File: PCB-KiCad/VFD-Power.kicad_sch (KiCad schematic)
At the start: 15 parts, among them IC1 74132D, IC3 ZXBM5210, U3 R-78B5.0-2.0

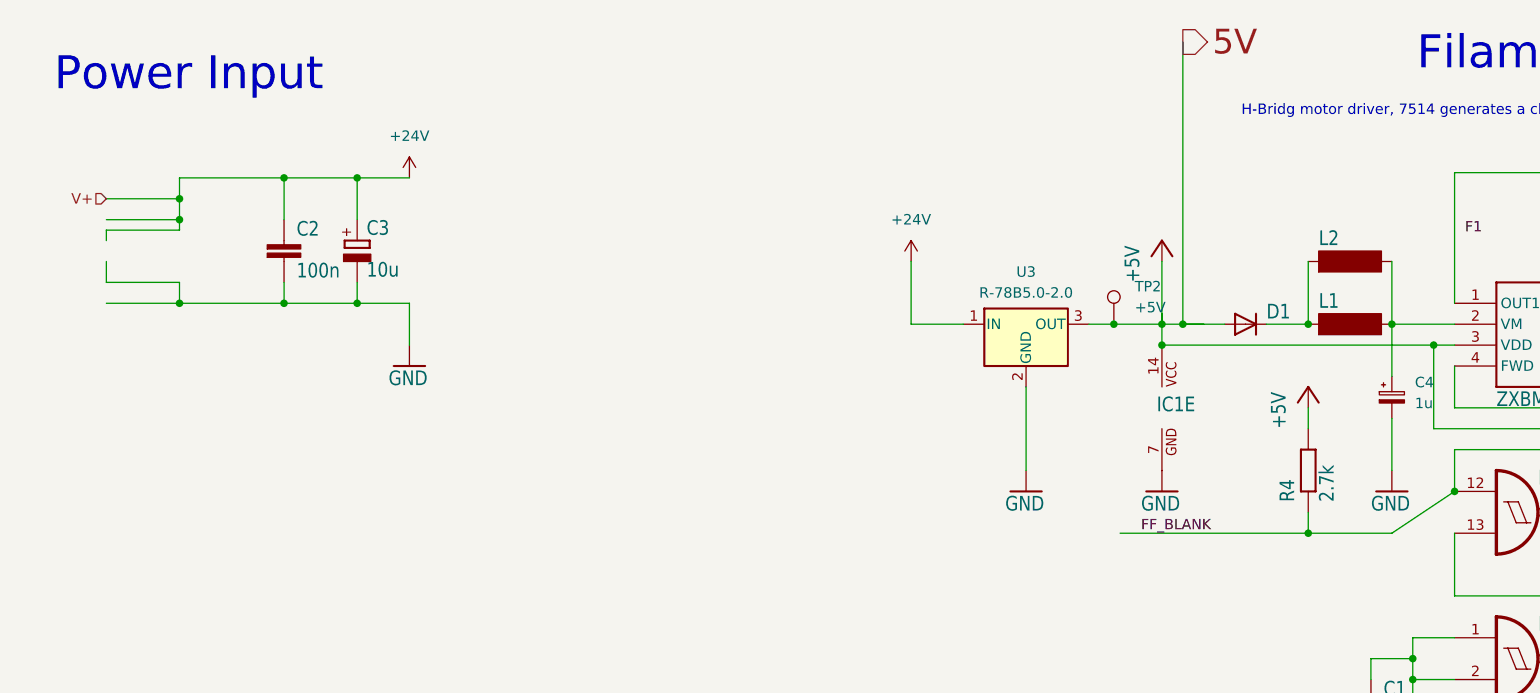
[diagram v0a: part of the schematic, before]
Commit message: GP1294 board, added light and remote sensors.
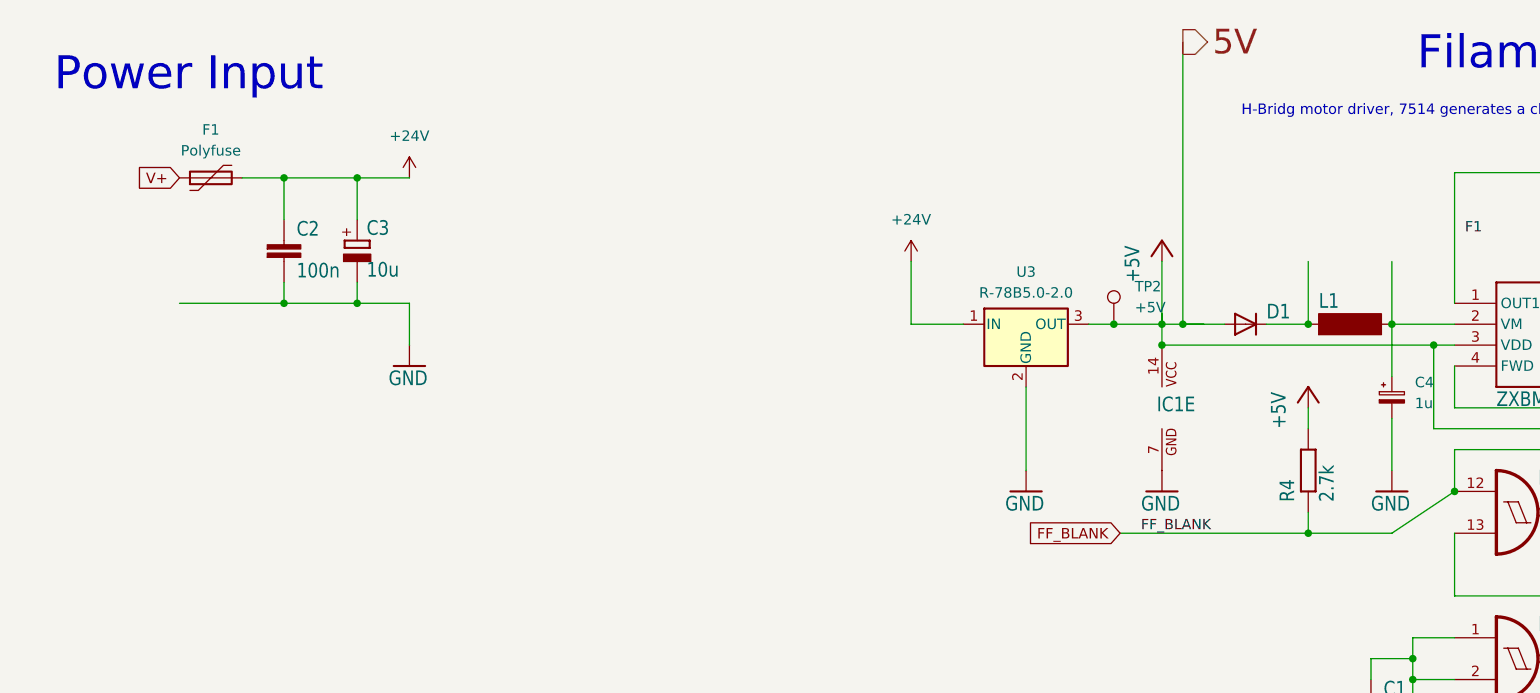
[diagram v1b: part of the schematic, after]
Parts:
- removed L2: MS85, VFD-Power:MS85, symbol VFD-Power-eagle-import:MS85
- added F1: Polyfuse, Fuse:Fuse_2920_7451Metric_Pad2.10x5.45mm_HandSolder, symbol Device:Polyfuse
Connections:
- net +24V: now also F1.2
- new net V+: F1.1
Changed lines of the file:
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@@
   (junction (at 191.77 96.52) (diameter 0) (color 0 0 0 0)
   )
-  (junction (at 41.91 38.1) (diameter 0) (color 0 0 0 0)
-  )
   (junction (at 179.07 53.34) (diameter 0) (color 0 0 0 0)
   )
@@
   (junction (at 63.5 50.8) (diameter 0) (color 0 0 0 0)
   )
+  (junction (at 54.61 35.56) (diameter 0) (color 0 0 0 0)
+  )
   (junction (at 155.448 53.34) (diameter 0) (color 0 0 0 0)
   )
-  (junction (at 54.61 35.56) (diameter 0) (color 0 0 0 0)
-  )
   (junction (at 217.17 93.98) (diameter 0) (color 0 0 0 0)
   )
@@
   (junction (at 161.29 55.88) (diameter 0) (color 0 0 0 0)
   )
-  (junction (at 41.91 50.8) (diameter 0) (color 0 0 0 0)
-  )
   (junction (at 194.31 55.88) (diameter 0) (color 0 0 0 0)
   )
-  (junction (at 41.91 40.64) (diameter 0) (color 0 0 0 0)
-  )
   (wire (pts (xy 155.448 53.34) (xy 161.29 53.34))
     (stroke (width 0) (type default))
@@
     (stroke (width 0.1524) (type solid))
   )
-  (wire (pts (xy 33.02 40.64) (xy 41.91 40.64))
-    (stroke (width 0) (type default))
-  )
-  (wire (pts (xy 41.91 41.91) (xy 41.91 40.64))
-    (stroke (width 0.1524) (type solid))
-  )
-  (wire (pts (xy 33.02 45.72) (xy 33.02 48.26))
-    (stroke (width 0.1524) (type solid))
-  )
   (wire (pts (xy 214.63 93.98) (xy 214.63 106.68))
     (stroke (width 0.1524) (type solid))
@@
     (stroke (width 0.1524) (type solid))
   )
-  (wire (pts (xy 33.02 38.1) (xy 41.91 38.1))
-    (stroke (width 0) (type default))
-  )
   (wire (pts (xy 255.27 38.735) (xy 255.27 42.545))
     (stroke (width 0) (type default))
@@
     (stroke (width 0.1524) (type solid))
   )
-  (wire (pts (xy 33.02 41.91) (xy 41.91 41.91))
-    (stroke (width 0.1524) (type solid))
-  )
   (wire (pts (xy 189.23 64.77) (xy 189.23 71.12))
     (stroke (width 0.1524) (type solid))
@@
     (stroke (width 0.1524) (type solid))
   )
+  (wire (pts (xy 49.53 35.56) (xy 54.61 35.56))
+    (stroke (width 0) (type default))
+  )
   (wire (pts (xy 189.23 53.34) (xy 196.85 53.34))
     (stroke (width 0.1524) (type solid))
@@
     (stroke (width 0.1524) (type solid))
   )
-  (wire (pts (xy 41.91 38.1) (xy 41.91 35.56))
-    (stroke (width 0.1524) (type solid))
-  )
   (wire (pts (xy 222.25 78.74) (xy 222.25 86.36))
     (stroke (width 0.1524) (type solid))
@@
     (stroke (width 0.1524) (type solid))
   )
-  (wire (pts (xy 41.91 40.64) (xy 41.91 38.1))
-    (stroke (width 0.1524) (type solid))
-  )
   (wire (pts (xy 161.29 45.72) (xy 161.29 53.34))
     (stroke (width 0.1524) (type solid))
@@
     (stroke (width 0.1524) (type solid))
   )
-  (wire (pts (xy 33.02 43.18) (xy 33.02 41.91))
-    (stroke (width 0.1524) (type solid))
-  )
   (wire (pts (xy 29.21 121.92) (xy 29.21 139.7))
     (stroke (width 0.1524) (type solid))
@@
     (stroke (width 0.1524) (type solid))
   )
-  (wire (pts (xy 41.91 35.56) (xy 54.61 35.56))
-    (stroke (width 0.1524) (type solid))
-  )
   (wire (pts (xy 189.23 45.72) (xy 189.23 53.34))
     (stroke (width 0.1524) (type solid))
@@
     (stroke (width 0) (type default))
   )
-  (wire (pts (xy 33.02 48.26) (xy 41.91 48.26))
-    (stroke (width 0.1524) (type solid))
-  )
   (wire (pts (xy 186.69 111.76) (xy 186.69 104.14))
     (stroke (width 0.1524) (type solid))
@@
     (stroke (width 0.1524) (type solid))
   )
-  (wire (pts (xy 33.02 50.8) (xy 41.91 50.8))
-    (stroke (width 0) (type default))
-  )
   (wire (pts (xy 222.25 50.8) (xy 240.03 50.8))
     (stroke (width 0.1524) (type solid))
@@
   )
   (wire (pts (xy 222.25 96.52) (xy 217.17 96.52))
-    (stroke (width 0.1524) (type solid))
-  )
-  (wire (pts (xy 41.91 48.26) (xy 41.91 50.8))
     (stroke (width 0.1524) (type solid))
   )
@@
   (label "FF_BLANK" (at 158.75 78.74 0) (fields_autoplaced)
     (effects (font (size 1.2446 1.2446)) (justify left bottom))
+  )
+  (global_label "FF_BLANK" (shape input) (at 156.21 78.74 180) (fields_autoplaced)
+    (effects (font (size 1.27 1.27)) (justify right))
+    (property "Intersheetrefs" "${INTERSHEET_REFS}" (at 144.0928 78.74 0)
+      (effects (font (size 1.27 1.27)) (justify right) hide)
+    )
   )
   (global_label "F1" (shape input) (at 254.635 31.75 0) (fields_autoplaced)
@@
     )
   )
+  (global_label "V+" (shape input) (at 41.91 35.56 180) (fields_autoplaced)
+    (effects (font (size 1.27 1.27)) (justify right))
+    (property "Intersheetrefs" "${INTERSHEET_REFS}" (at 36.2638 35.56 0)
+      (effects (font (size 1.27 1.27)) (justify right) hide)
+    )
+  )
   (hierarchical_label "F2" (shape output) (at 264.16 42.545 0) (fields_autoplaced)
     (effects (font (size 3 3)) (justify left))
@@
   (hierarchical_label "F1" (shape output) (at 264.16 34.925 0) (fields_autoplaced)
     (effects (font (size 3 3)) (justify left))
-  )
-  (hierarchical_label "V+" (shape input) (at 33.02 38.1 180) (fields_autoplaced)
-    (effects (font (size 1.27 1.27)) (justify right))
   )
   (hierarchical_label "5V" (shape output) (at 163.83 19.05 0) (fields_autoplaced)
@@
     )
   )
+  (symbol (lib_id "Device:Polyfuse") (at 45.72 35.56 90) (unit 1)
+    (in_bom yes) (on_board yes) (dnp no) (fields_autoplaced)
+    (property "Reference" "F1" (at 45.72 29.718 90)
+      (effects (font (size 1.27 1.27)))
+    )
+    (property "Value" "Polyfuse" (at 45.72 32.258 90)
+      (effects (font (size 1.27 1.27)))
+    )
+    (property "Footprint" "Fuse:Fuse_2920_7451Metric_Pad2.10x5.45mm_HandSolder" (at 50.8 34.29 0)
+      (effects (font (size 1.27 1.27)) (justify left) hide)
+    )
+    (property "Datasheet" "~" (at 45.72 35.56 0)
+      (effects (font (size 1.27 1.27)) hide)
+    )
+    (pin "1")
+    (pin "2")
+    (instances
+      (project "GP1294-Teens4"
+        (path "/3de011e3-f89b-42a8-8637-1f4c3f0867fa/9e049bd2-8c7e-4a7a-b856-b0fbd11ae8df"
+          (reference "F1") (unit 1)
+        )
+      )
+    )
+  )
   (symbol (lib_id "VFD-Power-eagle-import:R-EU_0411/15") (at 229.87 42.545 180) (unit 1)
     (in_bom yes) (on_board yes) (dnp no)
@@
         )
       )
-    )
-  )
-  (symbol (lib_id "VFD-Power-eagle-import:MS85") (at 184.15 45.72 0) (unit 1)
-    (in_bom yes) (on_board yes) (dnp no)
-    (property "Reference" "L2" (at 180.34 43.942 0)
-      (effects (font (size 1.778 1.5113)) (justify left bottom))
-    )
-    (property "Value" "MS85" (at 180.34 49.276 0)
-      (effects (font (size 1.778 1.5113)) (justify left bottom) hide)
-    )
-    (property "Footprint" "VFD-Power:MS85" (at 184.15 45.72 0)
-      (effects (font (size 1.27 1.27)) hide)
-    )
-    (property "Datasheet" "" (at 184.15 45.72 0)
-      (effects (font (size 1.27 1.27)) hide)
-    )
-    (pin "1")
-    (pin "2")
-    (instances
-      (project "GP1294-Teens4"
-        (path "/3de011e3-f89b-42a8-8637-1f4c3f0867fa/9e049bd2-8c7e-4a7a-b856-b0fbd11ae8df"
-          (reference "L2") (unit 1)
-        )
-      )
-      (project "VFD-Power"
-        (path "/d66e9896-ee3f-419d-ab82-78a854ae4100"
-          (reference "L2") (unit 1)
-        )
-      )

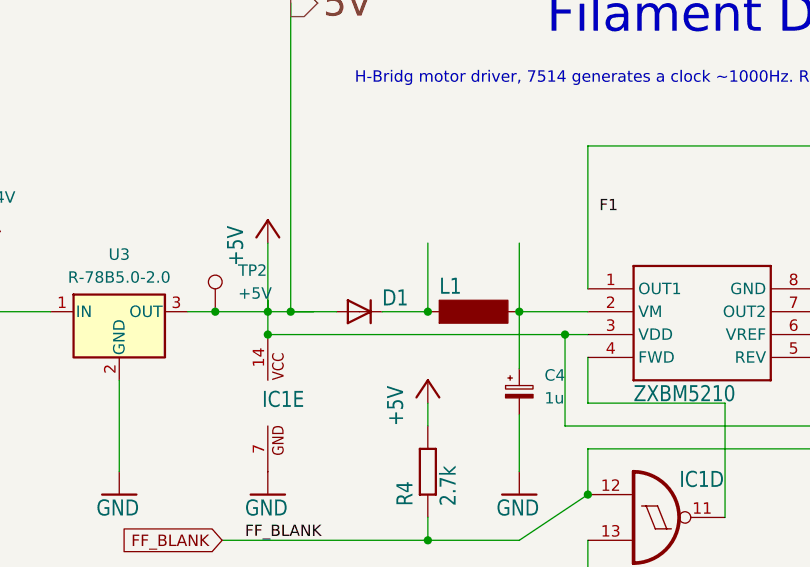
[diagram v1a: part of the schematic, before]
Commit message: Some silkscreen fixes.
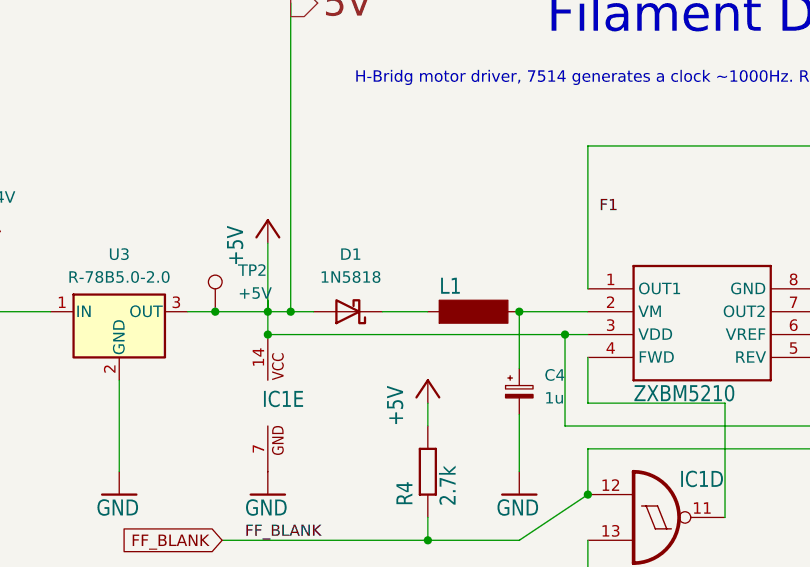
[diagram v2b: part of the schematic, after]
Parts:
- removed D1: DIODE-SMB, Diode_SMD:Nexperia_CFP3_SOD-123W, symbol VFD-Power:DIODE-SOD123
- added D1: 1N5818, Diode_SMD:D_SMA_Handsoldering, symbol Diode:1N5818
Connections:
- net +5V: now also D1.2 (A)
- net at L1.1: now also D1.1 (K)
